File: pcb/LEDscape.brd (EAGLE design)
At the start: 133.3 x 88.9 mm, 32 parts, among them IC1 MAX3041CUE, IC2 MAX3041CUE, IC3 MAX3041CUE, IC4 MAX3041CUE, IC5 MAX3041CUE, IC6 MAX3041CUE, IC7 MAX3041CUE, IC8 MAX3041CUE

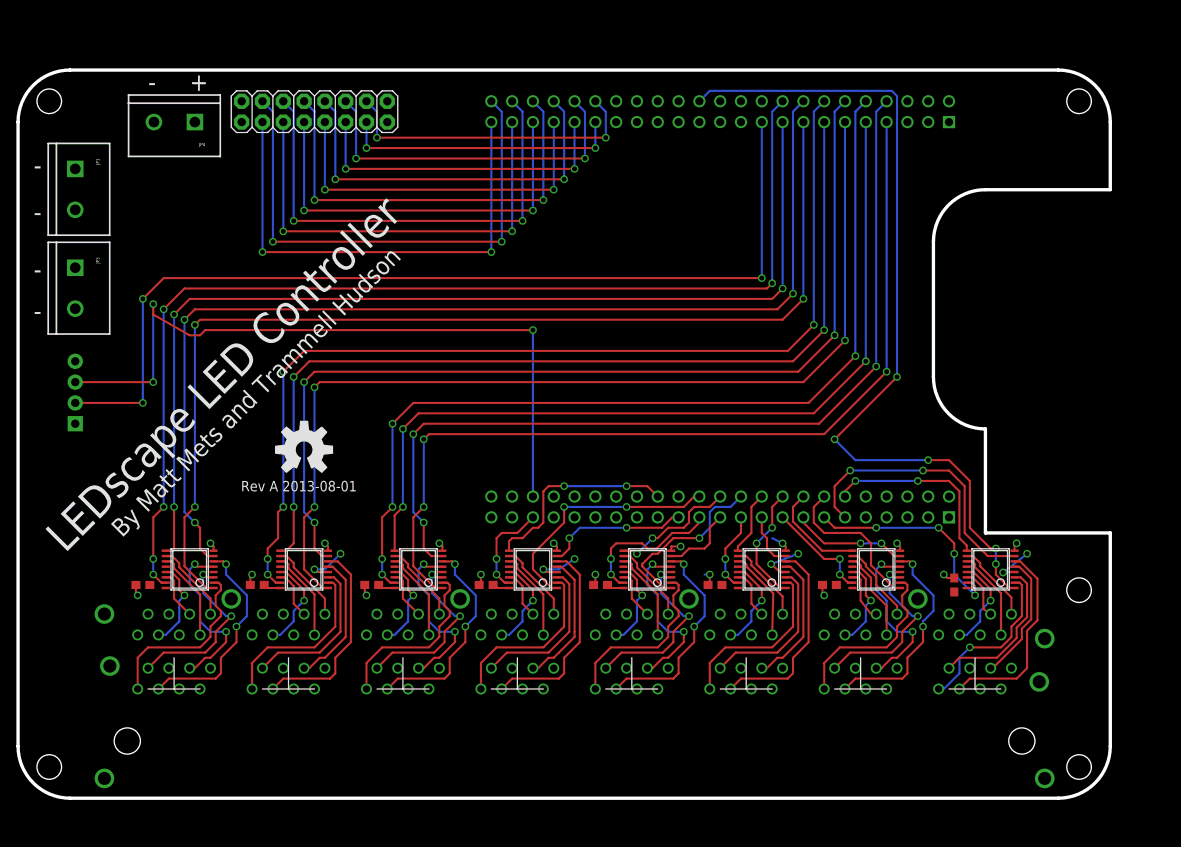
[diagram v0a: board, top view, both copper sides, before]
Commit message: RevB LEDscape board design: slightly bigger, debug headers for all signals
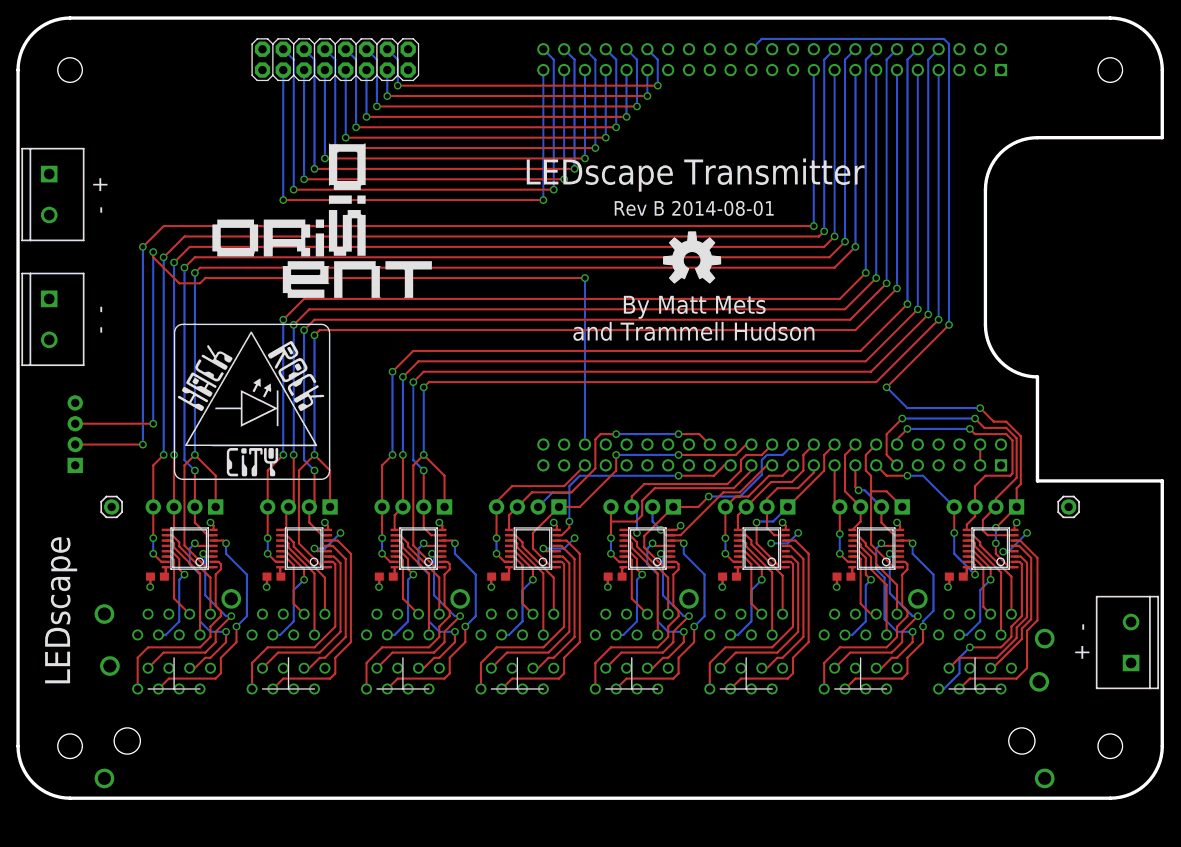
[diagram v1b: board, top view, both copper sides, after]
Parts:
- added JP10, JP11, JP12, JP2, JP6, JP7, JP8, JP9: (no value), SparkFun-Connectors:1X04_NO_SILK
- added JP13: (no value), SparkFun-Connectors:SCREWTERMINAL-5MM-2
- added JP15: M01PTH, SparkFun-Connectors:1X01
- added U$13: (no value), naim_misc:HRC_LOGO_0.75IN
- added U$14: (no value), naim_misc:DISORIENT_LOGO
- JP3: value (none) -> M01PTH; device SparkFun-Connectors:SCREWTERMINAL-5MM-2 -> SparkFun-Connectors:1X01
- moved U$11 52.7 mm to (82.3, 65.7)
- moved JP3 29.5 mm to (11.4, 35.6), turned to 0 degrees
- moved JP4 18.9 mm to (3.81, 76.2), turned to 270 degrees
- moved JP1 16.2 mm to (3.81, 61.0)
- moved U$1 8.98 mm to (139.1, 93.3)
- moved U$12 6.84 mm to (29.8, 88.9)
- moved JP5 5.08 mm to (6.99, 40.6)
- moved IC1 2.54 mm to (48.9, 30.5)
- moved IC2 2.54 mm to (34.9, 30.5)
- moved IC3 2.54 mm to (21.0, 30.5)
- moved IC4 2.54 mm to (118.7, 30.5)
- moved IC5 2.54 mm to (104.8, 30.5)
- moved IC6 2.54 mm to (90.8, 30.5)
- moved IC7 2.54 mm to (76.8, 30.5)
- moved IC8 2.54 mm to (62.9, 30.5)
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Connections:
- removed net VDD_5V: U$1.51, U$1.52
- new net SYS_5V: U$1.53
- net +5V: now also JP13.1, U$1.51, U$1.52; no longer U$1.53, U$1.54
- net GND: now also JP13.2, JP15.1; no longer JP3.2
- net S0: now also JP2.1
- net S1: now also JP2.2
- net S10: now also JP7.3
- net S11: now also JP7.4
- net S12: now also JP8.1
- net S13: now also JP8.2
- net S14: now also JP8.3
- net S15: now also JP8.4
- net S16: now also JP9.1
- net S17: now also JP9.2
- net S18: now also JP9.3
- net S19: now also JP9.4
- net S2: now also JP2.3
- net S20: now also JP10.1
- net S21: now also JP10.2
- net S22: now also JP10.3
- net S23: now also JP10.4
- net S24: now also JP11.1
- net S25: now also JP11.2
- net S26: now also JP11.3
- net S27: now also JP11.4
- net S28: now also JP12.1
- net S29: now also JP12.2
- net S3: now also JP2.4
- net S30: now also JP12.3
- net S31: now also JP12.4
- net S4: now also JP6.1
- net S5: now also JP6.2
- net S6: now also JP6.3
- net S7: now also JP6.4
- net S8: now also JP7.1
- net S9: now also JP7.2
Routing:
- net S4: track 120.4 -> 138.2 mm
- net EXTRA1: track 87.9 -> 105.7 mm
- net EXTRA0: track 116.6 -> 134.4 mm
- net S8: track 131.8 -> 149.4 mm
- net S0: track 111.1 -> 128.6 mm
- net S29: track 17.6 -> 32.3 mm
- net S25: track 9.05 -> 20.6 mm, vias 0 -> 1
- net S26: track 15.6 -> 27.0 mm, vias 2 -> 1
- net S5: track 119.1 -> 129.8 mm
- net S27: track 18.4 -> 29.1 mm
- net S3: track 112.5 -> 122.6 mm
- net S2: track 104.4 -> 114.6 mm
- net S7: track 122.5 -> 132.6 mm
- net S6: track 114.9 -> 125.0 mm
- net S10: track 125.6 -> 135.8 mm
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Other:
- board size 133.3 x 88.9 mm -> 139.7 x 95.2 mm
- board text added: "+ -"
- board text added: "- +"
- board text added: "- -"
- board text added: "LEDscape"
- board text added: "LEDscape Transmitter"
- board text added: "Rev B 2014-08-01"
- board text removed: "+"
- board text removed: "-"
- board text removed: "LEDscape LED Controller"
- board text removed: "Rev A 2013-08-01"

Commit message: Redesign transmitter PCB to use top and bottom ground planes, and one track for +5V- should be much easier to work with.
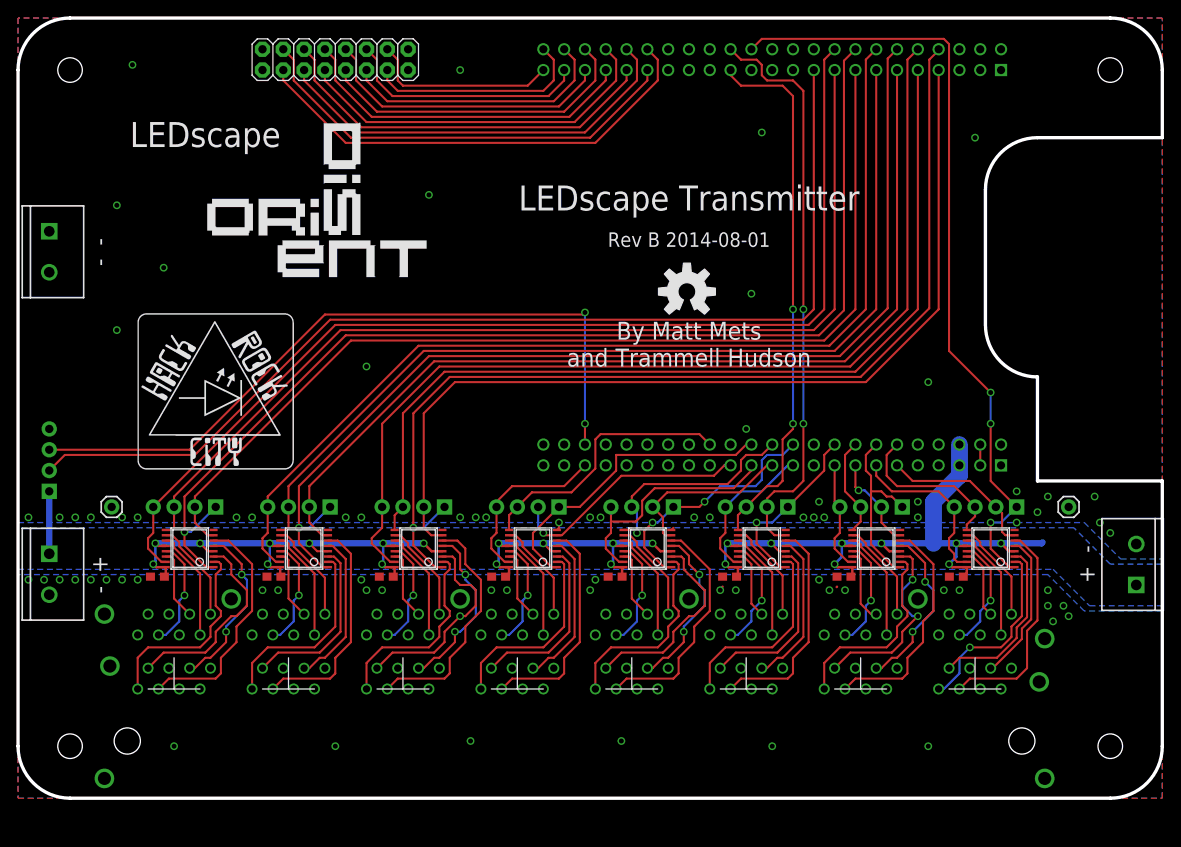
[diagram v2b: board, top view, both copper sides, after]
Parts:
- moved JP4 46.4 mm to (3.81, 29.8)
- moved U$12 18.0 mm to (47.6, 91.4), turned to 180 degrees
- moved JP13 9.55 mm to (136.5, 26.0)
- moved JP1 8.26 mm to (3.81, 69.2)
- moved U$13 4.62 mm to (14.6, 40.1)
- moved JP5 4.49 mm to (3.81, 37.5)
- moved U$11 3.86 mm to (81.7, 61.8)
- moved U$14 2.62 mm to (37.0, 71.1)
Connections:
- net +5V: no longer U$12.1, U$12.2
- net GND: now also U$12.1, U$12.2
- net S0: now also U$1.8; no longer U$1.7
- net S1: now also U$1.7; no longer U$1.8
- net S21: now also U$1.28; no longer U$1.65
- net S22: now also U$1.27; no longer U$1.66
- net S4: now also U$1.12; no longer U$1.11
- net S5: now also U$1.11; no longer U$1.12
- net S8: now also U$1.16; no longer U$1.15
- net S9: now also U$1.15; no longer U$1.16
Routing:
- net +5V: track 30.9 -> 187.8 mm, vias 8 -> 24
- net S21: track 14.1 -> 70.9 mm, vias 0 -> 2
- net S22: track 15.8 -> 65.8 mm, vias 0 -> 2
- net E0: track 63.5 -> 23.2 mm, vias 2 -> 0
- net E1: track 67.1 -> 27.0 mm, vias 2 -> 0
- net E3: track 62.0 -> 33.1 mm, vias 2 -> 0
- net E2: track 58.4 -> 30.0 mm, vias 2 -> 0
- net S13: track 39.1 -> 19.2 mm, vias 2 -> 0
- net E5: track 56.9 -> 39.2 mm, vias 2 -> 0
- net GND: track 19.0 -> 1.48 mm, vias 16 -> 78
- net EXTRA1: track 105.7 -> 88.5 mm, vias 3 -> 2
- net E4: track 53.3 -> 36.2 mm, vias 2 -> 0
- net E10: track 38.1 -> 54.6 mm, vias 2 -> 0
- net E11: track 41.7 -> 57.6 mm, vias 2 -> 0
- net S9: track 140.5 -> 125.4 mm, vias 3 -> 0
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- added copper zone on layer 16, net +5V
- added copper zone on layer 1, net GND
- removed copper zone on layer 1, net +5V

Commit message: Updated BBB footprint, mounting holes in LEDscape baord, small cleanups
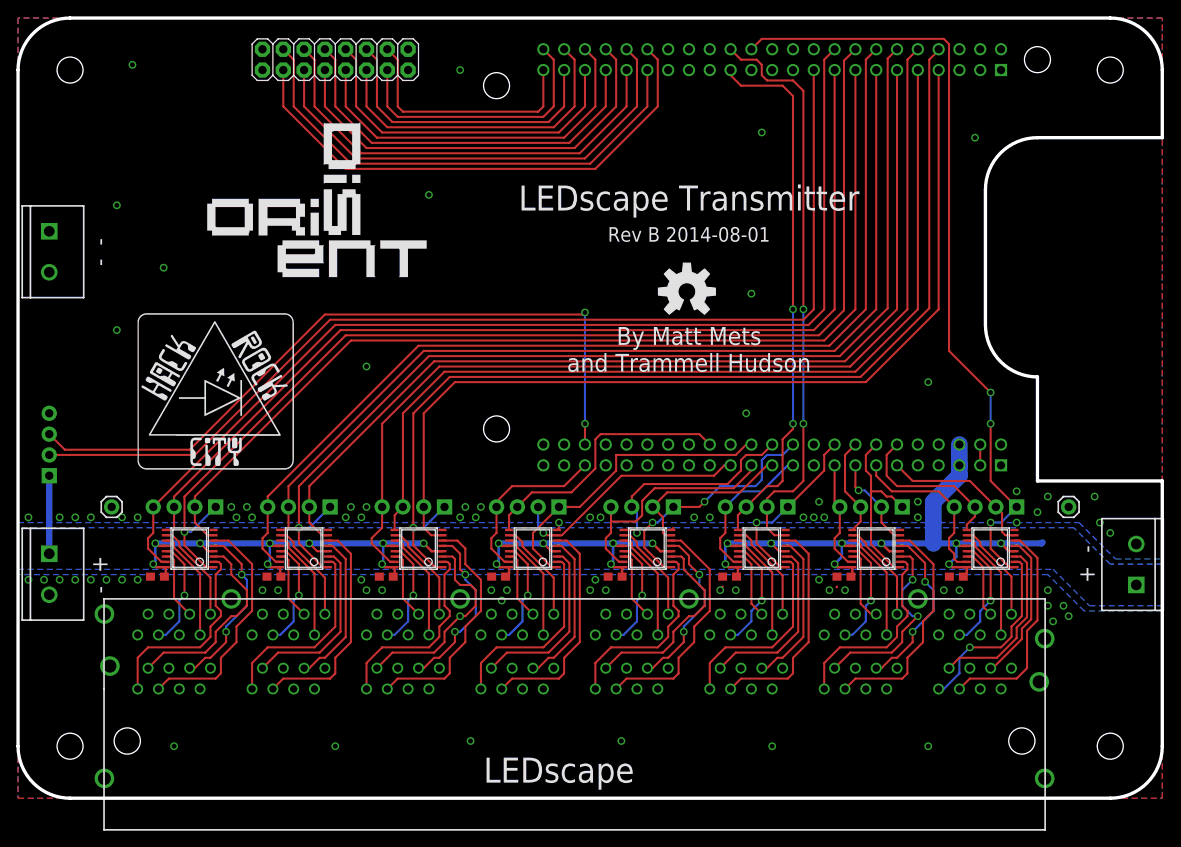
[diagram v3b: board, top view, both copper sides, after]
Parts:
- moved JP5 1.90 mm to (3.81, 39.4)
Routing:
- net E0: track 23.2 -> 30.3 mm
- net E11: track 57.6 -> 64.0 mm
- net E8: track 48.4 -> 54.8 mm
- net E9: track 51.5 -> 57.9 mm
- net E7: track 45.4 -> 51.7 mm
- net E6: track 42.3 -> 48.7 mm
- net E5: track 39.2 -> 45.6 mm
- net E4: track 36.2 -> 42.5 mm
- net E3: track 33.1 -> 39.5 mm
- net E2: track 30.0 -> 36.4 mm
- net E10: track 54.6 -> 60.9 mm
- net E1: track 27.0 -> 33.3 mm
- net +5V: track 187.8 -> 189.7 mm
- net EXTRA0: track 130.7 -> 129.9 mm
- net EXTRA1: track 88.5 -> 89.3 mm
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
